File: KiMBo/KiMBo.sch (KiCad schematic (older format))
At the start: 63 parts

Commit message: Annotate all components, now passing ERC, added ferrites to the rest of the connectors
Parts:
- added FB29, FB30, FB31, FB32, FB33, FB34, FB35, FB36, FB37, FB38, FB39: MMZ1608A252BTA00, symbol INDUCTOR_Small
- gave numbers to parts that had none: 63
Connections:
- net VDD_5V: now also FB37.1, FB38.1; no longer P16.1 (P1), P34.1 (P1)
- net ~SS_DOCK0_NVM: now also FB34.2; no longer P5.6 (P6)
- net ~SS_DOCK0_T: now also FB33.2; no longer P5.5 (P5)
- net ~SS_DOCK1_NVM: now also FB36.2; no longer P6.6 (P6)
- net ~SS_DOCK1_T: now also FB35.2; no longer P6.5 (P5)
- net ~SS_TOOLHEAD0_NVM: now also FB30.2; no longer P3.6 (P6)
- net ~SS_TOOLHEAD0_T: now also FB29.2; no longer P3.5 (P5)
- net ~SS_TOOLHEAD1_NVM: now also FB32.2; no longer P4.6 (P6)
- net ~SS_TOOLHEAD1_T: now also FB31.2; no longer P4.5 (P5)
- net at D5.1 (K), U1.4 (I/O_VCC): now also FB39.1; no longer P16.2 (P2)
- new net: FB39.2, P16.2 (P2)
- new net: FB38.2, P16.1 (P1)
- new net: FB30.1, P3.6 (P6)
- new net: FB29.1, P3.5 (P5)
- new net: FB31.1, P4.5 (P5)
- new net: FB32.1, P4.6 (P6)
- new net: FB33.1, P5.5 (P5)
- new net: FB34.1, P5.6 (P6)
- new net: FB35.1, P6.5 (P5)
- new net: FB36.1, P6.6 (P6)
- new net: FB37.2, P34.1 (P1)
- no-connect marks 1 -> 2
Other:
- note added: "Power"
- moved on the sheet: C1, C2, C3, C4, C5, CON1, D1, D2, D3, D4, D5, FB1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

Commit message: Clean up various parts of the schematic, high level sheet has annoated modules
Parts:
- renumbered C2 to C1, C1 to C2, FB2 to FB10, FB3 to FB11, FB4 to FB12, FB38 to FB13, FB39 to FB14, FB37 to FB15, FB29 to FB2, FB30 to FB3, FB31 to FB4, FB32 to FB5, FB33 to FB6, FB34 to FB7, FB35 to FB8, FB36 to FB9, P17 to P16, P18 to P17, P19 to P18, P20 to P19, P21 to P20, P22 to P21, P23 to P22, P24 to P23, P25 to P24, P26 to P25, P27 to P26, P28 to P27, P29 to P28, P30 to P29, P31 to P30, P32 to P31, P16 to P32
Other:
- note added: "&Config"
- note added: "User LEDs"
- note added: "eMMC"
- moved on the sheet: C1, C2, D1, D2, D3, D4, P11, P12, P13, R1, R2, R3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

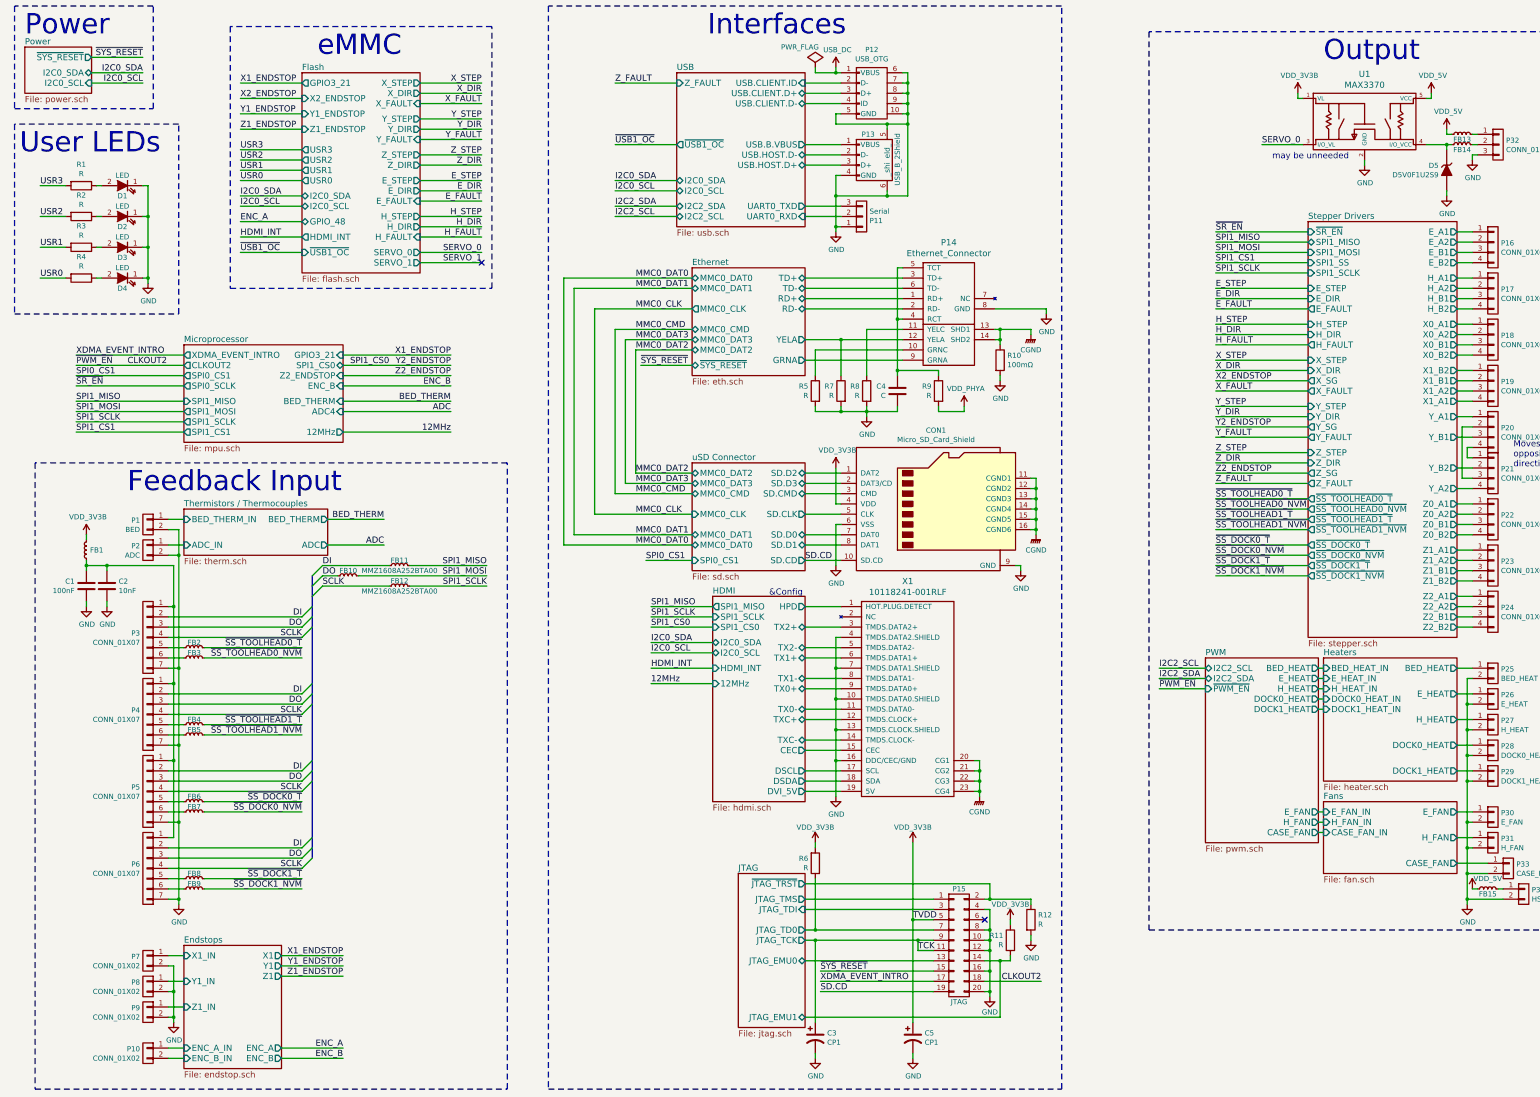
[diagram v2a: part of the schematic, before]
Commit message: Reorder the SS and EN lines from the shift registers such that the previously enabled/disabled motors stay enabled/disabled whilst writting to the shift register
Change 10k resistors to 4.7k, flip the open-drain inverter connected to B15 (PMTC_PGOOD)

Update the links in the README

Update the PDF schematic
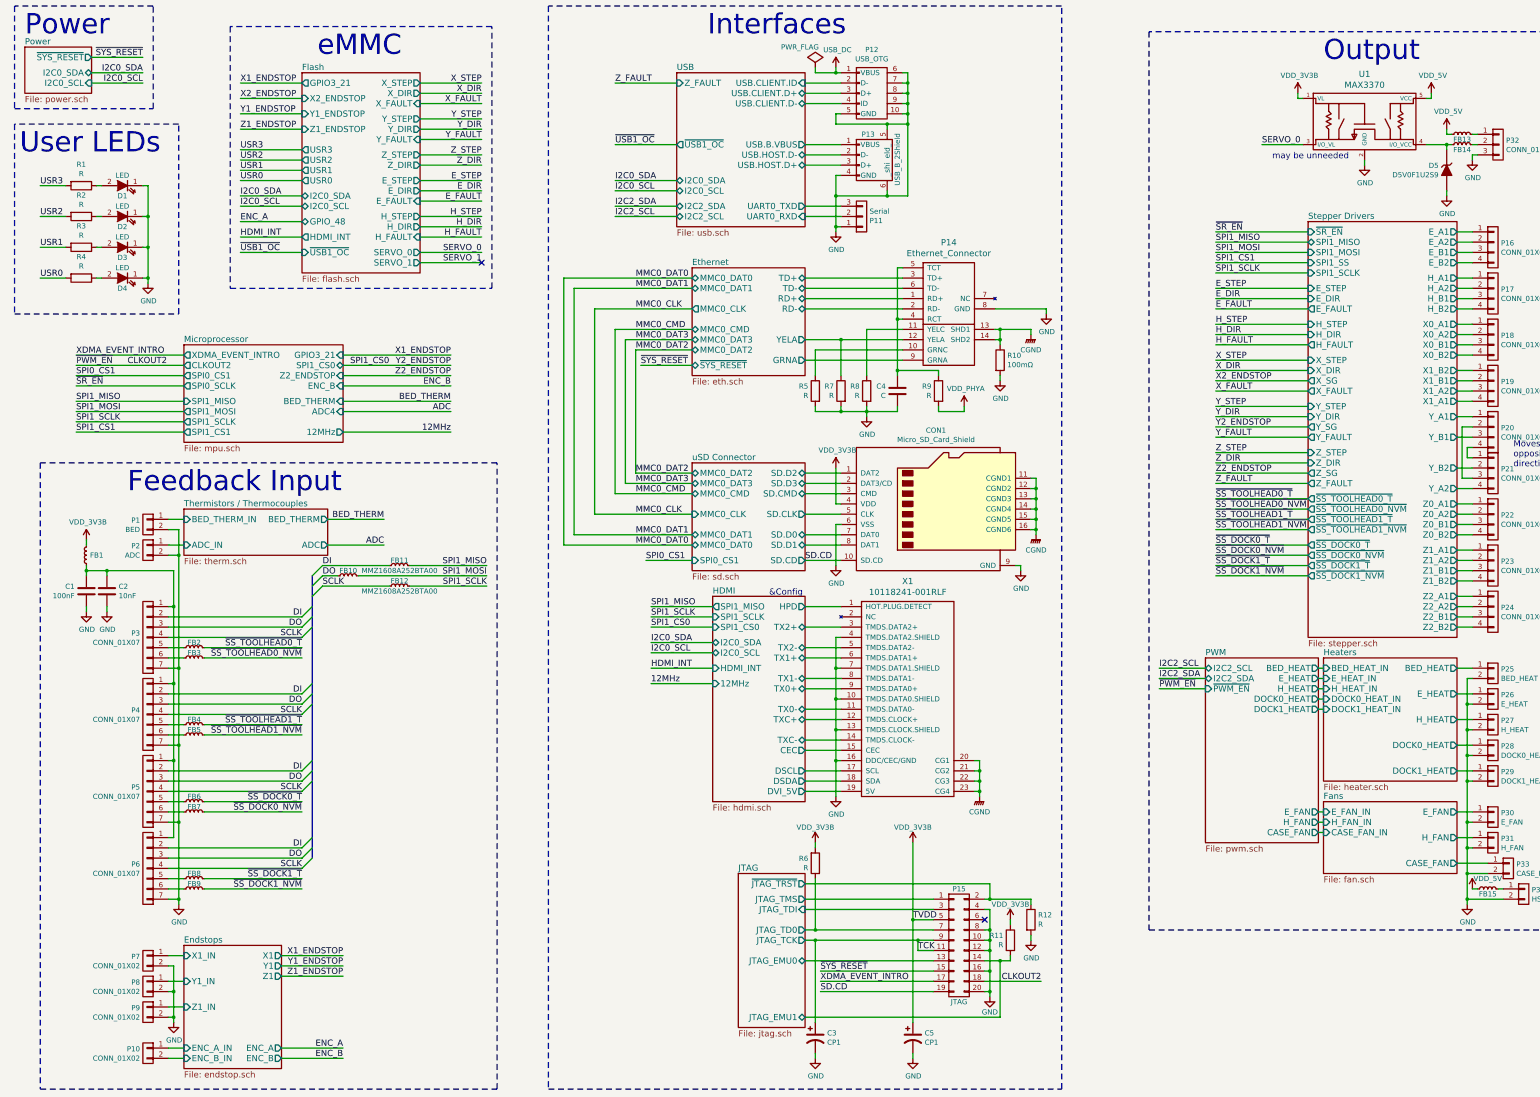
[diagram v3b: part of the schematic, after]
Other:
- moved on the sheet: C1, C2, FB1

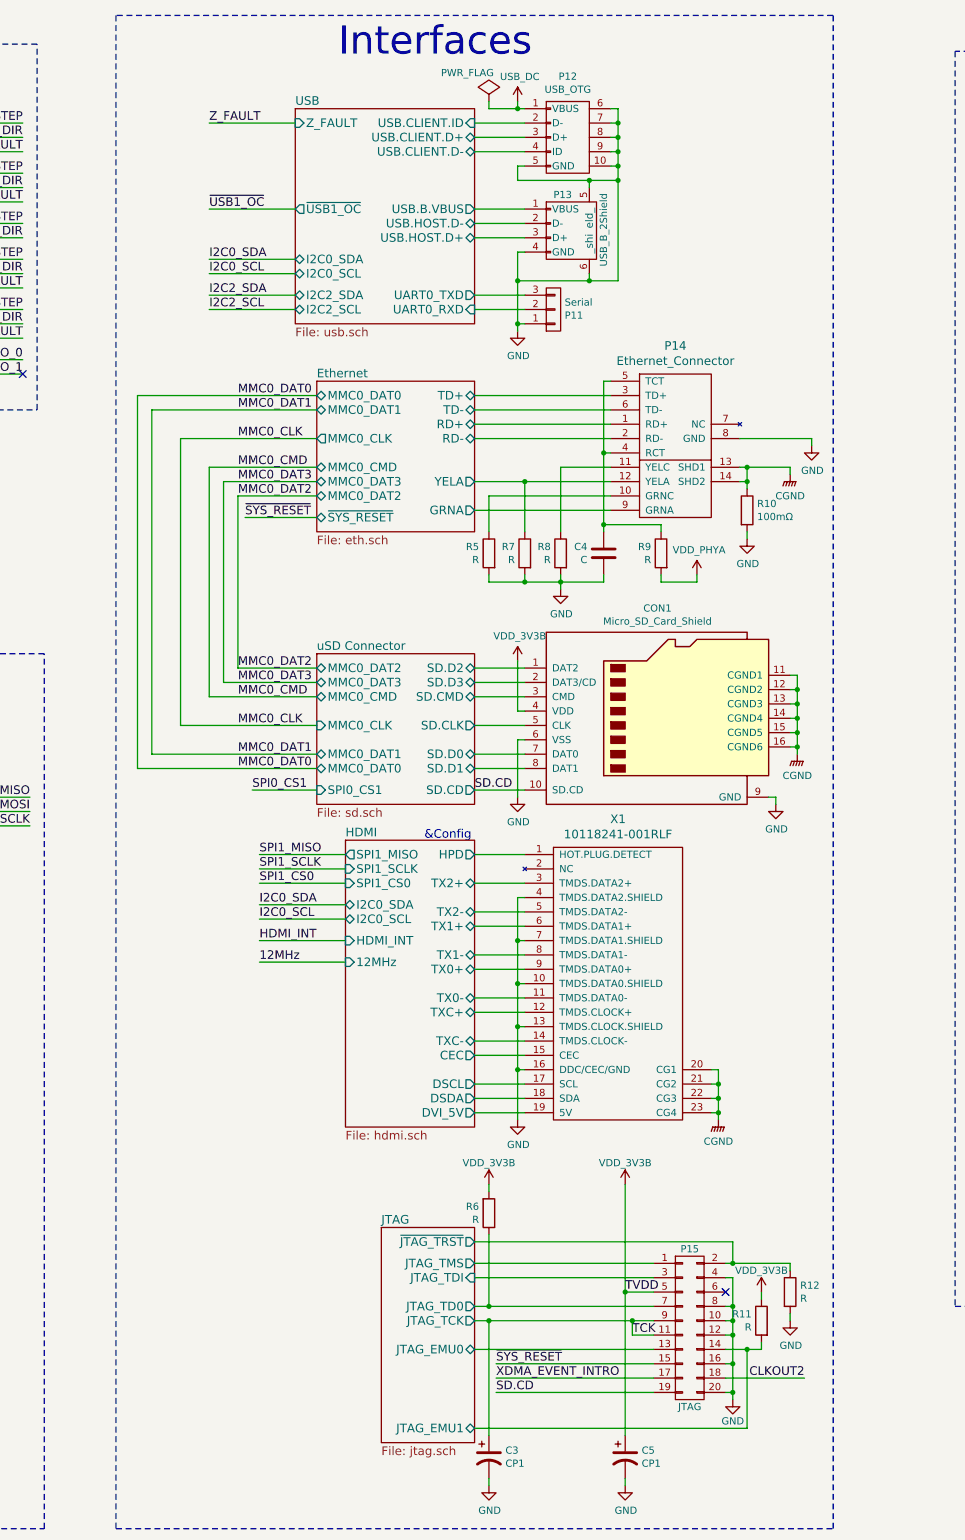
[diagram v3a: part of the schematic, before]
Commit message: Begin entry of component values
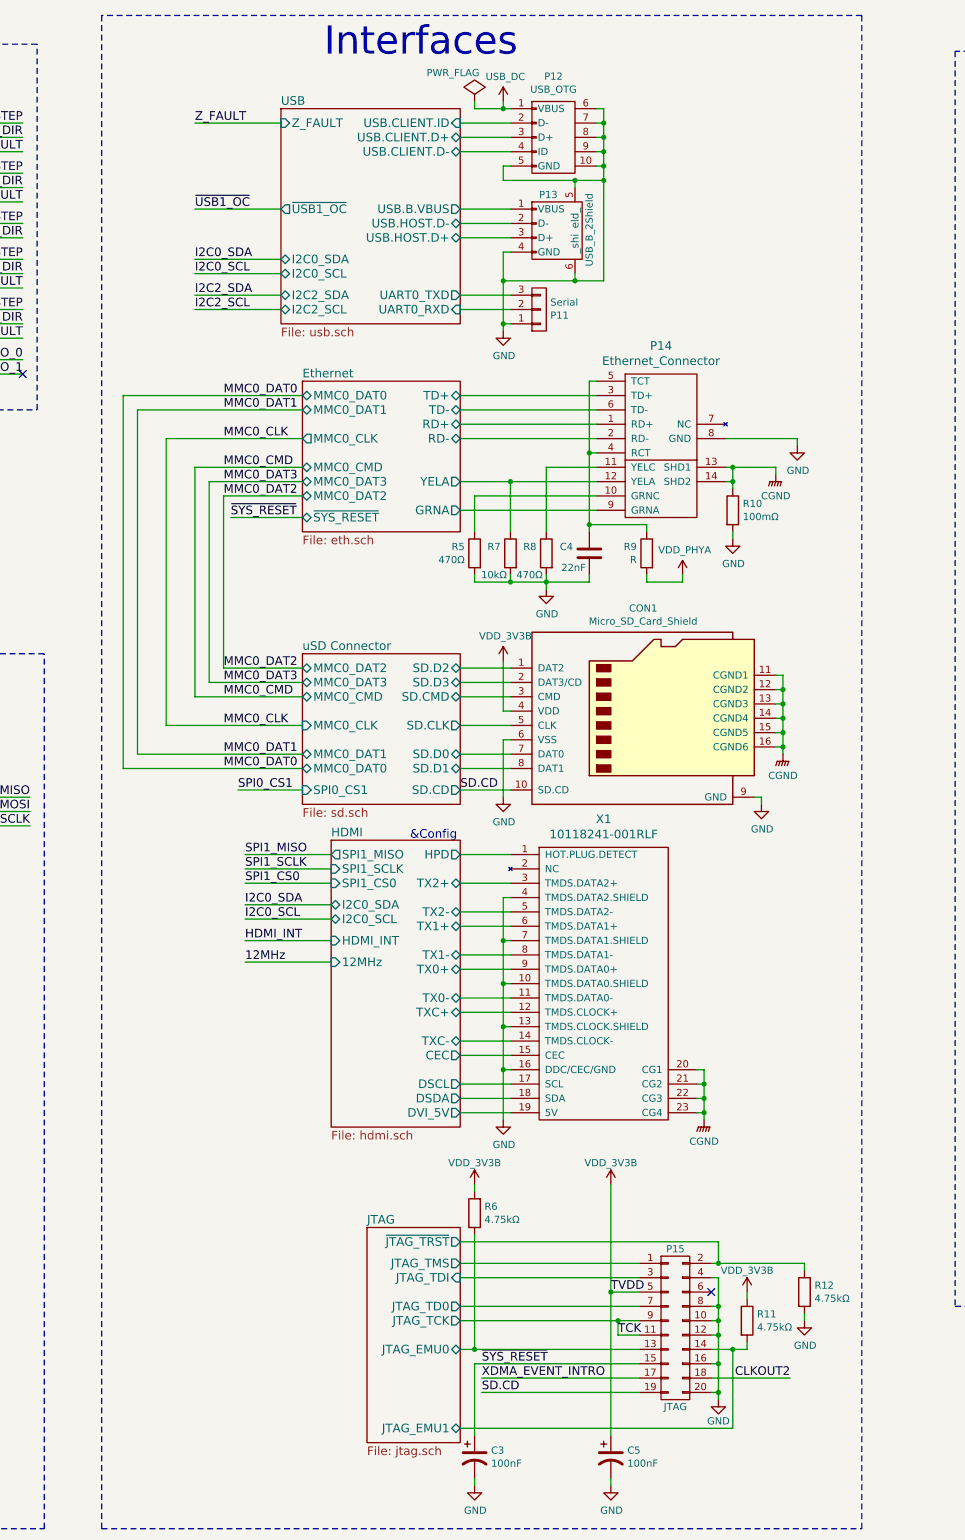
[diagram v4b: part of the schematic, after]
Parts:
- C3, C5: value CP1 -> 100nF
- C4: value C -> 22nF
- R11, R12, R6: value R -> 4.75kΩ
- R5, R8: value R -> 470Ω
- R7: value R -> 10kΩ
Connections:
- net JTAG/JTAG_EMU0: now also R6.1
- net JTAG/JTAG_TD0: no longer R6.1
- net TCK: no longer C3.1
- net ~SYS_RESET: now also C3.1
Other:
- moved on the sheet: C3, C4, C5, CON1, P11, P12, P13, P14, P15, R10, R11, R12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

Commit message: Entry of additional component values
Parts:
- CON1: value Micro_SD_Card_Shield -> μSD
- P12: value USB_OTG -> μUSB
- P13: value USB_B_2Shield -> USB_Type_A
- P14: value Ethernet_Connector -> Ethernet
- P32: value CONN_01X03 -> PWM
- R1, R2, R3, R4: value R -> 1kΩ
- R9: value R -> 0Ω
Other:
- moved on the sheet: P11, P12, P13
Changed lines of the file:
@@
 L USB_B_2Shield P13
 U 1 1 58E3EAE7
-P 8850 2050
-F 0 "P13" H 8750 2300 50  0000 L CNN
-F 1 "USB_B_2Shield" V 9100 1800 50  0000 L CNN
-F 2 "" V 8850 1950 50  0001 C CNN
-F 3 "" V 8850 1950 50  0000 C CNN
-	1    8850 2050
+P 8800 2050
+F 0 "P13" H 8700 2300 50  0000 L CNN
+F 1 "USB_Type_A" V 9050 1825 50  0000 L CNN
+F 2 "" V 8800 1950 50  0001 C CNN
+F 3 "" V 8800 1950 50  0000 C CNN
+	1    8800 2050
 	1    0    0    -1
 $EndComp
@@
 L USB_OTG_5_SHIELD_PINS P12
 U 1 1 58E440E1
-P 8850 1400
-F 0 "P12" V 8425 1400 50  0000 C CNN
-F 1 "USB_OTG" V 8516 1400 50  0000 C CNN
-F 2 "" V 8800 1300 50  0001 C CNN
-F 3 "" V 8800 1300 50  0000 C CNN
-	1    8850 1400
+P 8800 1400
+F 0 "P12" V 8375 1400 50  0000 C CNN
+F 1 "μUSB" V 8466 1400 50  0000 C CNN
+F 2 "" V 8750 1300 50  0001 C CNN
+F 3 "" V 8750 1300 50  0000 C CNN
+	1    8800 1400
 	0    1    1    0
 $EndComp
@@
 P 9450 5400
 F 0 "CON1" H 9475 6117 50  0000 C CNN
-F 1 "Micro_SD_Card_Shield" H 9475 6026 50  0000 C CNN
+F 1 "μSD" H 9475 6026 50  0000 C CNN
 F 2 "" H 10600 5700 50  0001 C CNN
 F 3 "" H 9450 5400 50  0000 C CNN
@@
 P 9600 3550
 F 0 "P14" H 9600 4247 60  0000 C CNN
-F 1 "Ethernet_Connector" H 9600 4141 60  0000 C CNN
+F 1 "Ethernet" H 9600 4141 60  0000 C CNN
 F 2 "" H 9600 4150 60  0001 C CNN
 F 3 "http://www.link-pp.com/?product/201411246424.html" H 9600 4150 60  0001 C CNN
@@
 P 9500 4300
 F 0 "R9" H 9569 4346 50  0000 L CNN
-F 1 "R" H 9569 4255 50  0000 L CNN
+F 1 "0Ω" H 9569 4255 50  0000 L CNN
 F 2 "" V 9430 4300 50  0001 C CNN
 F 3 "" H 9500 4300 50  0000 C CNN
@@
 L CONN_01X03 P11
 U 1 1 591BD471
-P 8750 2600
-F 0 "P11" H 8828 2641 50  0000 L CNN
-F 1 "Serial" H 8828 2550 50  0000 L CNN
-F 2 "" H 8750 2600 50  0001 C CNN
-F 3 "" H 8750 2600 50  0000 C CNN
-	1    8750 2600
+P 8700 2600
+F 0 "P11" H 8778 2641 50  0000 L CNN
+F 1 "Serial" H 8778 2550 50  0000 L CNN
+F 2 "" H 8700 2600 50  0001 C CNN
+F 3 "" H 8700 2600 50  0000 C CNN
+	1    8700 2600
 	1    0    0    1
 $EndComp
@@
 L GND #PWR016
 U 1 1 591BEB60
-P 8500 2750
-F 0 "#PWR016" H 8500 2500 50  0001 C CNN
-F 1 "GND" H 8505 2577 50  0000 C CNN
-F 2 "" H 8500 2750 50  0000 C CNN
-F 3 "" H 8500 2750 50  0000 C CNN
-	1    8500 2750
+P 8450 2750
+F 0 "#PWR016" H 8450 2500 50  0001 C CNN
+F 1 "GND" H 8455 2577 50  0000 C CNN
+F 2 "" H 8450 2750 50  0000 C CNN
+F 3 "" H 8450 2750 50  0000 C CNN
+	1    8450 2750
 	1    0    0    -1
 $EndComp
@@
 P 1250 2300
 F 0 "R1" V 1043 2300 50  0000 C CNN
-F 1 "R" V 1134 2300 50  0000 C CNN
+F 1 "1kΩ" V 1134 2300 50  0000 C CNN
 F 2 "" V 1180 2300 50  0001 C CNN
 F 3 "" H 1250 2300 50  0000 C CNN
@@
 P 1250 2600
 F 0 "R2" V 1043 2600 50  0000 C CNN
-F 1 "R" V 1134 2600 50  0000 C CNN
+F 1 "1kΩ" V 1134 2600 50  0000 C CNN
 F 2 "" V 1180 2600 50  0001 C CNN
 F 3 "" H 1250 2600 50  0000 C CNN
@@
 P 1250 2900
 F 0 "R3" V 1043 2900 50  0000 C CNN
-F 1 "R" V 1134 2900 50  0000 C CNN
+F 1 "1kΩ" V 1134 2900 50  0000 C CNN
 F 2 "" V 1180 2900 50  0001 C CNN
 F 3 "" H 1250 2900 50  0000 C CNN
@@
 P 1250 3200
 F 0 "R4" V 1043 3200 50  0000 C CNN
-F 1 "R" V 1134 3200 50  0000 C CNN
+F 1 "1kΩ" V 1134 3200 50  0000 C CNN
 F 2 "" V 1180 3200 50  0001 C CNN
 F 3 "" H 1250 3200 50  0000 C CNN
@@
 L USB_DC #PWR019
 U 1 1 59F95A45
-P 8500 1150
-F 0 "#PWR019" H 8500 1000 50  0001 C CNN
-F 1 "USB_DC" H 8515 1323 50  0000 C CNN
-F 2 "" H 8500 1150 50  0000 C CNN
-F 3 "" H 8500 1150 50  0000 C CNN
-	1    8500 1150
+P 8450 1150
+F 0 "#PWR019" H 8450 1000 50  0001 C CNN
+F 1 "USB_DC" H 8450 1300 50  0000 C CNN
+F 2 "" H 8450 1150 50  0000 C CNN
+F 3 "" H 8450 1150 50  0000 C CNN
+	1    8450 1150
 	1    0    0    -1
 $EndComp
@@
 P 15050 1900
 F 0 "P32" H 15128 1941 50  0000 L CNN
-F 1 "CONN_01X03" H 15128 1850 50  0000 L CNN
+F 1 "PWM" H 15128 1850 50  0000 L CNN
 F 2 "" H 15050 1900 50  0001 C CNN
 F 3 "" H 15050 1900 50  0000 C CNN
@@
 L PWR_FLAG #FLG035
 U 1 1 5BB43269
-P 8300 1150
-F 0 "#FLG035" H 8300 1245 50  0001 C CNN
-F 1 "PWR_FLAG" H 8150 1350 50  0000 C CNN
-F 2 "" H 8300 1150 50  0000 C CNN
-F 3 "" H 8300 1150 50  0000 C CNN
-	1    8300 1150
+P 8250 1150
+F 0 "#FLG035" H 8250 1245 50  0001 C CNN
+F 1 "PWR_FLAG" H 8250 1375 50  0000 C CNN
+F 2 "" H 8250 1150 50  0000 C CNN
+F 3 "" H 8250 1150 50  0000 C CNN
+	1    8250 1150
 	1    0    0    -1
 $EndComp
@@
 	14650 4400 14800 4400
 Wire Wire Line
-	9000 2400 9000 2350
-Wire Wire Line
-	9000 1750 9000 1700
-Wire Wire Line
-	9200 1700 8500 1700
-Wire Wire Line
-	8550 1300 8200 1300
-Wire Wire Line
-	8550 1400 8200 1400
-Wire Wire Line
-	8550 1500 8200 1500
-Wire Wire Line
-	8500 1600 8550 1600
-Wire Wire Line
-	8500 2200 8500 2750
-Wire Wire Line
-	8500 2200 8550 2200
-Wire Wire Line
-	9150 1200 9200 1200
-Wire Wire Line
-	9200 1600 9150 1600
-Wire Wire Line
-	9200 1500 9150 1500
-Connection ~ 9200 1500
-Wire Wire Line
-	9200 1400 9150 1400
-Connection ~ 9200 1400
-Wire Wire Line
-	9150 1300 9200 1300
-Connection ~ 9200 1300
-Connection ~ 9200 1600
-Connection ~ 9200 1700
-Wire Wire Line
-	9200 2400 8500 2400
-Connection ~ 9000 2400
-Wire Wire Line
-	8500 1150 8500 1200
-Wire Wire Line
-	8300 1200 8550 1200
-Wire Wire Line
-	8550 2000 8200 2000
-Wire Wire Line
-	8550 2100 8200 2100
-Wire Wire Line
-	8550 1900 8200 1900
+	8950 2400 8950 2350
+Wire Wire Line
+	8950 1750 8950 1700
+Wire Wire Line
+	9150 1700 8450 1700
+Wire Wire Line
+	8500 1300 8200 1300
+Wire Wire Line
+	8500 1400 8200 1400
+Wire Wire Line
+	8500 1500 8200 1500
+Wire Wire Line
+	8450 1600 8500 1600
+Wire Wire Line
+	8450 2200 8450 2750
+Wire Wire Line
+	8450 2200 8500 2200
+Wire Wire Line
+	9100 1200 9150 1200
+Wire Wire Line
+	9150 1600 9100 1600
+Wire Wire Line
+	9150 1500 9100 1500
+Connection ~ 9150 1500
+Wire Wire Line
+	9150 1400 9100 1400
+Connection ~ 9150 1400
+Wire Wire Line
+	9100 1300 9150 1300
+Connection ~ 9150 1300
+Connection ~ 9150 1600
+Connection ~ 9150 1700
+Wire Wire Line
+	9150 2400 8450 2400
+Connection ~ 8950 2400
+Wire Wire Line
+	8450 1150 8450 1200
+Wire Wire Line
+	8250 1200 8500 1200
+Wire Wire Line
+	8500 2000 8200 2000
+Wire Wire Line
+	8500 2100 8200 2100
+Wire Wire Line
+	8500 1900 8200 1900
 Wire Wire Line
 	10400 5250 10450 5250
@@
 	9750 4500 9750 4450
 Wire Wire Line
-	8500 1700 8500 1600
-Connection ~ 9000 1700
+	8450 1700 8450 1600
+Connection ~ 8950 1700
 Wire Wire Line
 	8550 5100 8200 5100
@@
 Connection ~ 2200 9250
 Wire Wire Line
-	8500 2700 8550 2700
-Connection ~ 8500 2700
-Connection ~ 8500 2400
-Wire Wire Line
-	9200 1200 9200 2400
-Wire Wire Line
-	8550 2500 8200 2500
-Wire Wire Line
-	8550 2600 8200 2600
+	8450 2700 8500 2700
+Connection ~ 8450 2700
+Connection ~ 8450 2400
+Wire Wire Line
+	9150 1200 9150 2400
+Wire Wire Line
+	8500 2500 8200 2500
+Wire Wire Line
+	8500 2600 8200 2600
 Wire Wire Line
 	2250 10700 2100 10700
@@
 	8550 8200 8200 8200
 Wire Wire Line
-	8300 1200 8300 1150
-Connection ~ 8500 1200
+	8250 1200 8250 1150
+Connection ~ 8450 1200
 Wire Wire Line
 	3800 4700 4850 4700
